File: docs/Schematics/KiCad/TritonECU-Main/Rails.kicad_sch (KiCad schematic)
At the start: 3 parts

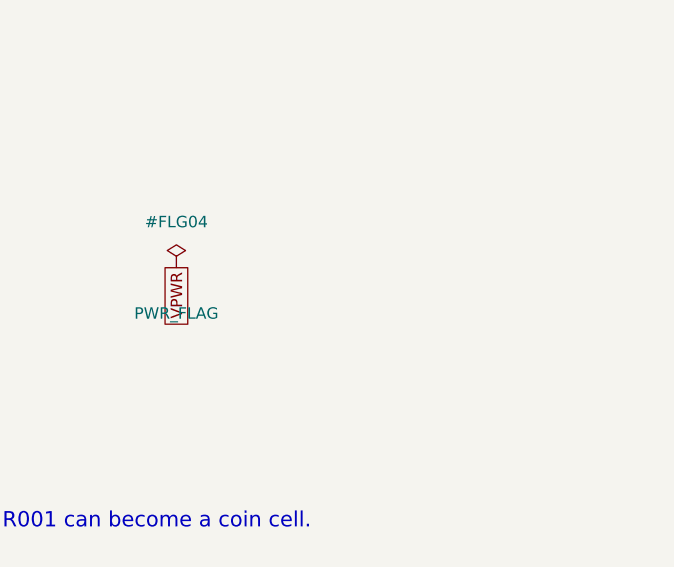
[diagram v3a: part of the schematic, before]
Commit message: Carrier: VREF sheet, and the power board's +VIN is VPROT, not VPWR
VREF: NCV8772C 5.00 V on the protected rail, EN from the MCU; TPS2H160B-Q1
at 248 mA per feed, latch mode; LM74700-Q1 + DMN6040 ideal diode and
SMAJ24CA per feed; 100k/12.4k short-to-battery sense. Channel 2 drawn,
not fitted (one VREF pin, 90).

Fix: power board J3 +VIN is the LTC4364 OUTPUT (IC1 pin 1, after R2).
The carrier had it on VPWR, joining the surge stopper's output to its
raw input. It is now its own net, VPROT, which also feeds VREF.

gen_carrier_pcb.py: no-connect pins get their unconnected net (parity),
and --replace-sheet NAME re-places one sheet's parts.

Co-Authored-By: Claude Opus 5.5 <noreply@anthropic.com>
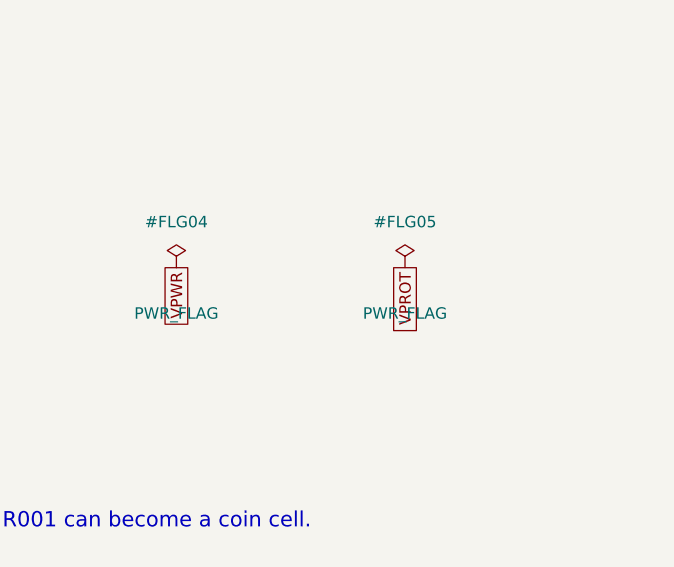
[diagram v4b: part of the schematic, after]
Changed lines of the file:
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@@
 	)
 	(global_label "VPWR" (shape passive) (at 116.84 50.80 270) (effects (font (size 1.27 1.27)) (justify right)))
+	(symbol (lib_id "power:PWR_FLAG") (at 142.24 50.80 0) (unit 1)
+		(exclude_from_sim no) (in_bom no) (on_board yes) (dnp no)
+		(property "Reference" "#FLG05" (at 142.24 45.72 0) (effects (font (size 1.27 1.27))))
+		(property "Value" "PWR_FLAG" (at 142.24 55.88 0) (effects (font (size 1.27 1.27))))
+		(property "Footprint" "" (at 142.24 50.80 0) (hide yes) (effects (font (size 1.27 1.27))))
+		(property "Datasheet" "" (at 142.24 50.80 0) (hide yes) (effects (font (size 1.27 1.27))))
+		(pin "1")
+		(instances (project "TritonECU-Main" (path "/eec527cb-b372-4ed4-ac2b-16ccf6980056/6b17a514-781a-5b5f-b620-33ff1a7235d5" (reference "#FLG05") (unit 1))))
+	)
+	(global_label "VPROT" (shape passive) (at 142.24 50.80 270) (effects (font (size 1.27 1.27)) (justify right)))
 	(text "Bulk where the rails arrive from the power board connector." (exclude_from_sim no) (at 20.00 120.00 0) (effects (font (size 1.7 1.7)) (justify left bottom)))
 	(symbol (lib_id "Device:C") (at 50.80 139.70 0) (unit 1)

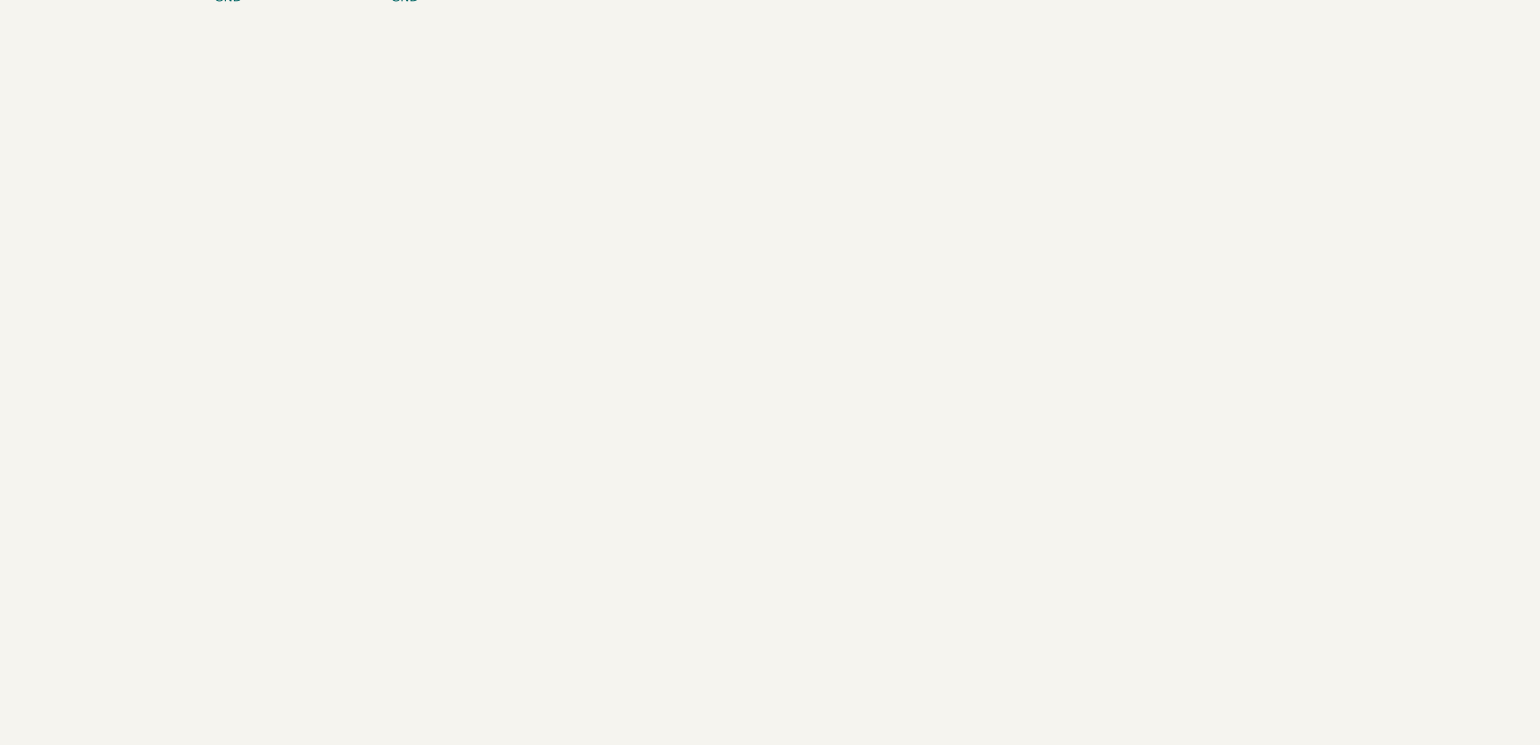
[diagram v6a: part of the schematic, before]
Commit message: Carrier: Inputs sheet and switched rails for sleep
Inputs: one network per switch input - 4.7k pull-up to VPWR (ground-
switched only; VPWR so a TR bit closed in Park draws nothing parked),
SMF24A, 33k/15k, 10n, BAT54J to 3.3 V. TR1/2/4 and 4X4L ground-switched,
TR3A/BRAKE/ACP/TCS 12 V high-side. 4X4L mapped to EEC-V pin 14
(findings sec.14). IGN_WAKE from VPWR into PC13/WKUP4. TACH/SPEED bench
header, BOOT0 DFU solder jumper.

Switched rails: +5V and +3.3V stay up parked, so two TPS22917 load
switches on SW_RAIL_EN (PG12, 100k down) make +5V_SW / +3.3V_SW for the
running-only loads: 74HCT541 x3 and OE pull-ups, MAX9926 x3 and COUT
pull-ups, ADS8588H, OPA2376 x2, O2 bias, knock block, 74HC4051, TPS2H160B
FAULT pull-up, TFT pull-up. MCU, watchdog, CAN, SCP RX, clamps stay on.

gen_carrier_pcb.py: packer steps around existing parts, fills several
rects in turn, parks overflow below earlier parked parts.

Co-Authored-By: Claude Opus 5.5 <noreply@anthropic.com>
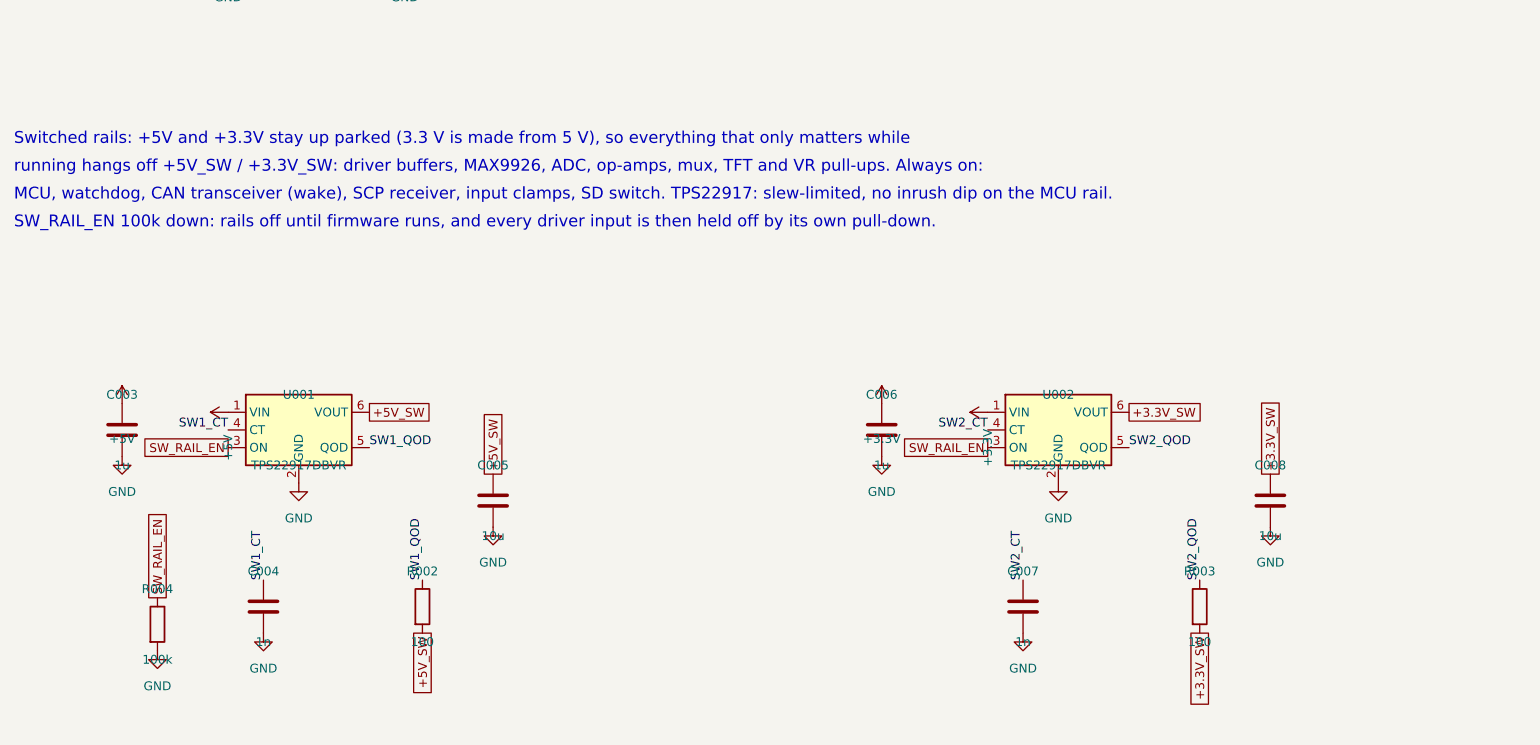
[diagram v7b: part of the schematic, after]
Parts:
- added C003, C006: 1u, Capacitor_SMD:C_0805_2012Metric_Pad1.18x1.45mm_HandSolder, symbol Device:C
- added C004, C007: 1n, Capacitor_SMD:C_0603_1608Metric_Pad1.08x0.95mm_HandSolder, symbol Device:C
- added C005, C008: 10u, Capacitor_SMD:C_0805_2012Metric_Pad1.18x1.45mm_HandSolder, symbol Device:C
- added R002, R003: 100, Resistor_SMD:R_0603_1608Metric_Pad0.98x0.95mm_HandSolder, symbol Device:R
- added R004: 100k, Resistor_SMD:R_0603_1608Metric_Pad0.98x0.95mm_HandSolder, symbol Device:R
- added U001, U002: TPS22917DBVR, Package_TO_SOT_SMD:SOT-23-6, symbol Power_Management:TPS22917DBV
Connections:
- net +3.3V: now also C006.1, U002.1 (VIN)
- net +5V: now also C003.1, U001.1 (VIN)
- net GND: now also C003.2, C004.2, C005.2, C006.2, C007.2, C008.2, R004.2, U001.2 (GND), U002.2 (GND)
- new net +3.3V_SW: C008.1, R003.2, U002.6 (VOUT)
- new net +5V_SW: C005.1, R002.2, U001.6 (VOUT)
- new net SW1_CT: C004.1, U001.4 (CT)
- new net SW1_QOD: R002.1, U001.5 (QOD)
- new net SW2_CT: C007.1, U002.4 (CT)
- new net SW2_QOD: R003.1, U002.5 (QOD)
- new net SW_RAIL_EN: R004.1, U001.3 (ON), U002.3 (ON)
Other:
- note added: "MCU, watchdog, CAN transceiver (wake), SCP receiver, input clamps, SD switch. TPS22917: slew-limited, no inrush dip on the MCU rail."
- note added: "SW_RAIL_EN 100k down: rails off until firmware runs, and every driver input is then held off by its own pull-down."
- note added: "Switched rails: +5V and +3.3V stay up parked (3.3 V is made from 5 V), so everything that only matters while"
- note added: "running hangs off +5V_SW / +3.3V_SW: driver buffers, MAX9926, ADC, op-amps, mux, TFT and VR pull-ups. Always on:"
